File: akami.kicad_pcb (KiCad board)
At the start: 4 copper layers, 30 x 33.3 mm, 64 parts, among them J1 USB_C_Receptacle_USB2.0, J2 Conn_01x01, J3 Conn_01x01, Q2 AO3401A, U1 nRF52840, U2 TP4054, U3 LP5912-3.3DRV, U4 ProMicro_2, Y1 32MHz, Y2 32.768 kHz

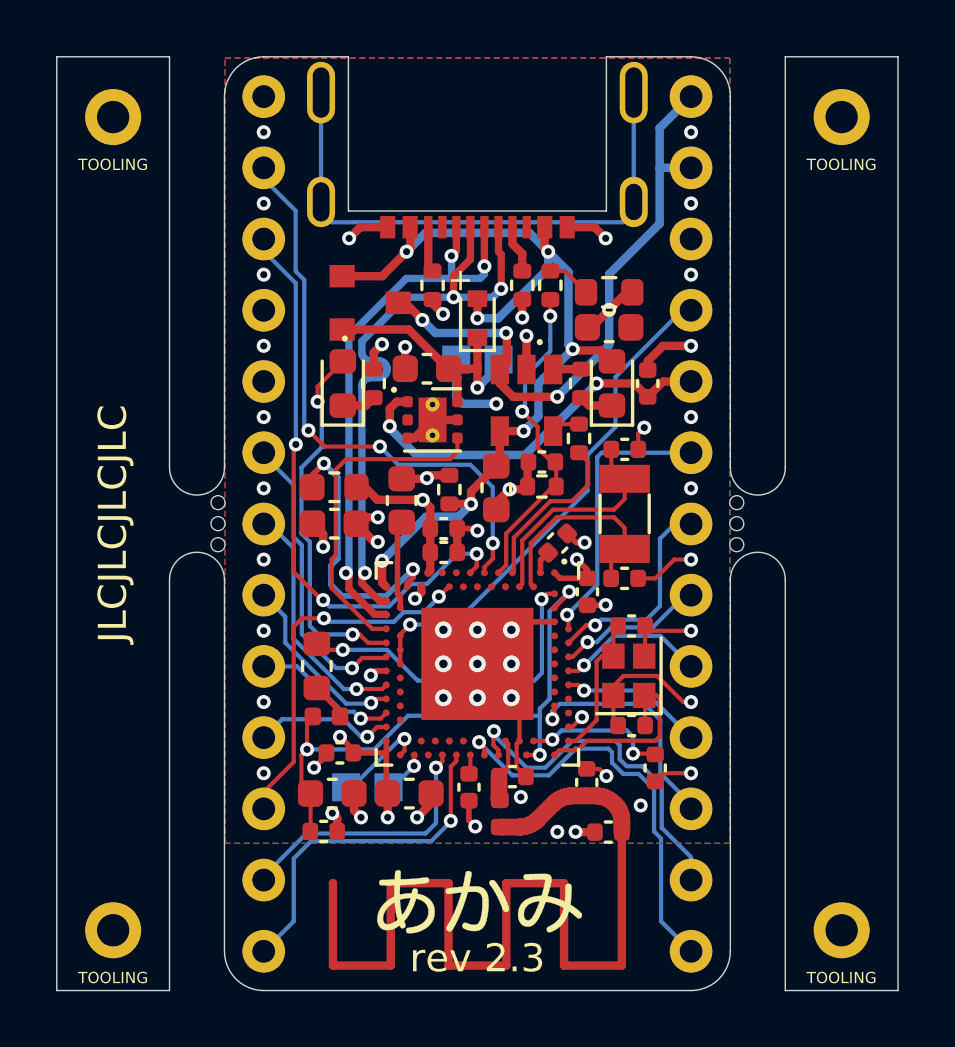
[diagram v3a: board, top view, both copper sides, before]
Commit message: continue placement and routing on 3A
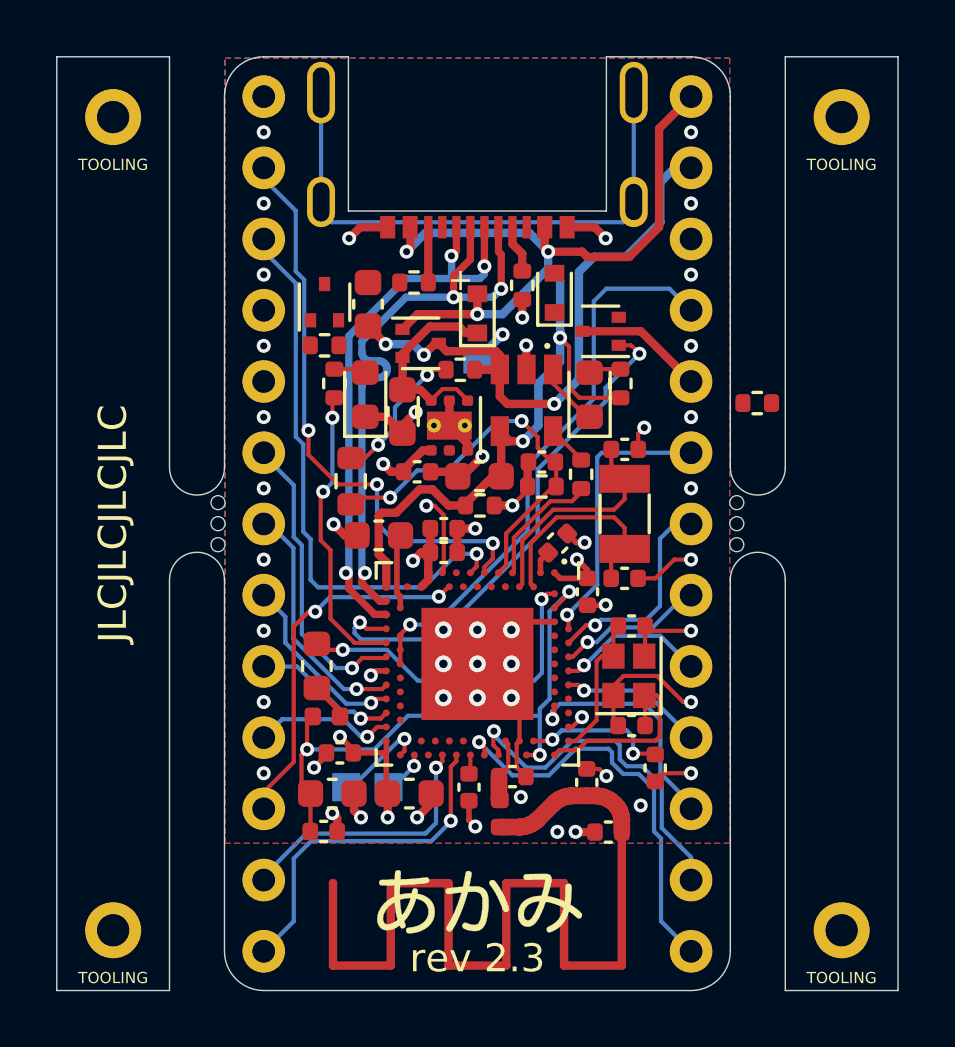
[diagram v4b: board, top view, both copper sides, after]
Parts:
- removed C23: 4.7uF, Capacitor_SMD:C_0603_1608Metric
- removed L4: 10uH, Inductor_SMD:L_0603_1608Metric
- removed TP5: TestPoint, TestPoint:TestPoint_Pad_1.0x1.0mm
- added D4: MSK4010, Diode_SMD:D_SOD-523, F.Cu at (2.75, -8.23)
- added Q1: DMP21D0UT, Package_TO_SOT_SMD:SOT-523, F.Cu at (4.39, -6.86)
- added Q3: DMP21D0UT, Package_TO_SOT_SMD:SOT-523, F.Cu at (-5.45, -7.90)
- added R1: 100k, Resistor_SMD:R_0402_1005Metric, F.Cu at (9.98, -4.30)
- added R2: 100k, Resistor_SMD:R_0402_1005Metric, F.Cu at (-5.45, -6.36)
- D2: value 1N5817 -> MSK4010
- Q2: value AO3401A -> DMP21D0UT; footprint Package_TO_SOT_SMD:SOT-23 -> Package_TO_SOT_SMD:SOT-523
- moved R11 11.4 mm to (-4.52, -1.51), turned to 270 degrees
- moved C24 8.81 mm to (-2.15, -1.85), turned to 0 degrees
- moved C21 8.64 mm to (-3.90, -7.83), turned to 270 degrees
- moved R3 4.40 mm to (-0.61, -5.49), turned to 180 degrees
- moved Q2 2.31 mm to (-2.02, -6.43)
- moved C20 1.76 mm to (-2.67, -4.00), turned to 90 degrees
- moved C13 1.49 mm to (-3.52, 0.42), turned to 180 degrees
- moved R5 1.40 mm to (-5.10, -5.00)
- moved R8 1.40 mm to (5.10, -5.00)
- moved R7 1.28 mm to (3.70, -1.76)
- moved R6 1.23 mm to (0.09, -0.65), turned to 0 degrees
- moved D1 0.89 mm to (-4.00, -4.60)
- moved D3 0.89 mm to (4.00, -4.60)
- moved TP3 0.76 mm to (0.00, -5.85)
- moved C14 0.73 mm to (0.07, -1.69), turned to 0 degrees
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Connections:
- C20 pad 2: VDD_HV -> Net-(C20-Pad2)
- C24 pad 1: EXT_VCC -> VDD_NRF
- D1 pad 1: Net-(D1-Pad1) -> GND
- D1 pad 2: BLUE_LED -> Net-(D1-Pad2)
- D2 pad 1: VDD_HV -> Net-(C20-Pad2)
- D3 pad 2: VBUS -> Net-(D3-Pad2)
- J2 pad 1: VBAT -> VBUS
- J3 pad 1: GND -> EXT_VCC
- Q2 pad 2: VDD_HV -> Net-(C20-Pad2)
- R11 pad 1: VBAT -> Net-(R11-Pad1)
- R11 pad 2: Net-(R11-Pad2) -> BAT_VOLT
- R3 pad 1: Net-(R11-Pad2) -> VBAT
- R3 pad 2: BAT_VOLT -> Net-(R11-Pad1)
- R5 pad 1: GND -> Net-(D1-Pad2)
- R5 pad 2: Net-(D1-Pad1) -> BLUE_LED
- R8 pad 1: Net-(R8-Pad1) -> Net-(D3-Pad2)
- R8 pad 2: Net-(D3-Pad1) -> VBUS
- U1 pad AD8: POWER_CTRL -> PPH_VCC_CTRL
- U1 pad Y2: VDD_HV -> VDD_NRF
- U2 pad 1: Net-(R8-Pad1) -> Net-(D3-Pad1)
- U3 pad 1: EXT_VCC -> VDD_NRF
- U3 pad 4: POWER_CTRL -> Net-(C20-Pad2)
- U3 pad 6: VDD_HV -> Net-(C20-Pad2)
- U4 pad 21: EXT_VCC -> PPH_VCC
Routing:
- net VDD_HV: track 23.4 -> 0.00 mm, vias 4 -> 0
- net PPH_VCC_CTRL: track 0.00 -> 19.2 mm, vias 0 -> 2
- net EXT_VCC: track 14.1 -> 0.00 mm, vias 2 -> 0
- net VBUS: track 33.4 -> 45.8 mm, vias 7 -> 5
- net POWER_CTRL: track 11.9 -> 0.00 mm
- net Net-(U1-PadAB2): track 9.85 -> 0.00 mm, vias 2 -> 0
- net Net-(C20-Pad2): track 0.00 -> 7.30 mm
- net Net-(R11-Pad1): track 0.00 -> 5.14 mm, vias 0 -> 2
- net PPH_VCC: track 0.00 -> 4.61 mm
- net VBAT: track 24.4 -> 21.4 mm, vias 4 -> 3
- net Net-(U1-PadU1): track 0.00 -> 2.84 mm, vias 0 -> 1
- net BLUE_LED: track 13.3 -> 10.6 mm
- net BAT_VOLT: track 11.6 -> 14.2 mm
- net RESET: track 18.0 -> 20.3 mm
- net GND: track 40.5 -> 38.5 mm, vias 53 -> 51
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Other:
- board text added: "VCC"
- board text removed: "H"
- board text removed: "L"

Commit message: rev 3 (lv): 1. layout and route all components
2. replace mosfet pullups with 1M resistors

3. silkscreen pin labelling now shows nRF52 pin numbers instead
   of promicro pins (those are "standard" and hence useless to
   print)

4. VBUS and EXT_VCC is now broken out; VBUS is coincidentally in
   the same place as an Elite-C (above RAW -- now BAT)

gerbers, BOM, and PnP files *are* updated.
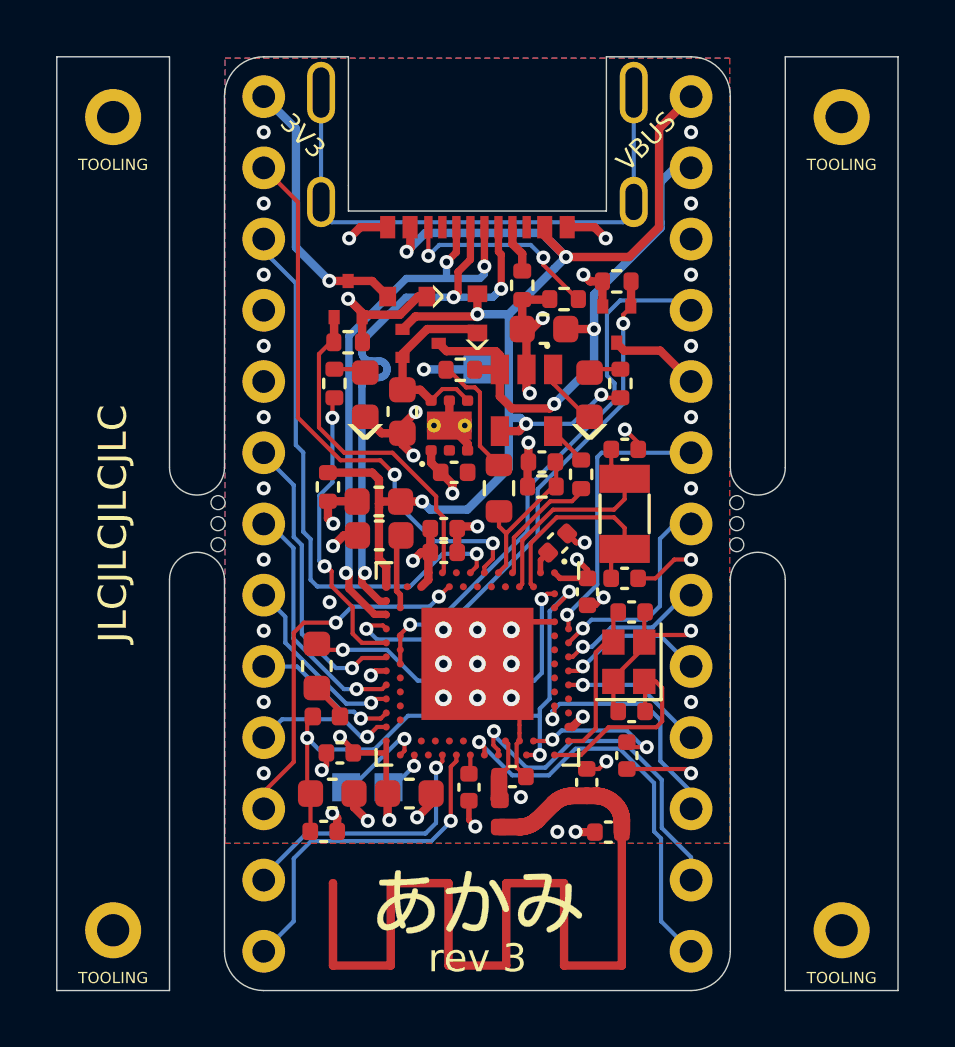
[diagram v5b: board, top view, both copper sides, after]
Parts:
- R1, R2: value 100k -> 1M
- U4: footprint footprints:promicro_no_silk -> footprints:akami-pins
- moved R1 6.63 mm to (4.97, -8.64)
- moved C21 6.34 mm to (2.38, -6.94), turned to 0 degrees
- moved R6 5.46 mm to (-5.33, -1.31), turned to 270 degrees
- moved R10 5.38 mm to (3.09, -8.01)
- moved R11 5.30 mm to (0.77, -1.26)
- moved D4 5.25 mm to (-2.50, -8.10), turned to 180 degrees
- moved C14 3.70 mm to (-3.52, -0.79)
- moved C24 1.32 mm to (-0.83, -1.83)
- moved C11 1.10 mm to (5.33, 8.27)
- moved Q3 0.85 mm to (-4.61, -8.01)
- moved R2 0.85 mm to (-4.61, -6.47)
- moved Q1 0.62 mm to (4.97, -7.10), turned to 270 degrees
- moved C6 0.50 mm to (5.50, 6.70)
- moved C7 0.50 mm to (5.50, 3.15)
- moved Y1 0.50 mm to (5.40, 4.92)
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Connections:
- net P1.10 renamed Net-(U1-PadA20)
- U1 pad U1: Net-(U1-PadU1) -> EXT_VCC_CTRL
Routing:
- net EXT_VCC_CTRL: track 0.00 -> 12.3 mm
- net EXT_VCC: track 0.00 -> 9.85 mm, vias 0 -> 1
- net BAT_VOLT: track 14.2 -> 5.78 mm, vias 2 -> 0
- net VDD_NRF: track 14.4 -> 21.0 mm, vias 8 -> 10
- net Net-(J1-PadB5): track 1.97 -> 7.50 mm, vias 0 -> 2
- net GND: track 38.5 -> 41.8 mm, vias 51 -> 52
- net Net-(U1-PadU1): track 2.84 -> 0.00 mm, vias 1 -> 0
- net VBAT: track 21.4 -> 18.7 mm, vias 3 -> 2
- net VBUS: track 45.8 -> 47.3 mm, vias 5 -> 6
- net PPH_VCC: track 4.61 -> 3.24 mm
- net P0.06: track 20.8 -> 20.0 mm, vias 3 -> 2
- net Net-(R11-Pad1): track 5.14 -> 4.42 mm, vias 2 -> 0
- net RESET: track 20.3 -> 19.6 mm
- net Net-(C7-Pad1): track 5.23 -> 5.79 mm
- net PPH_VCC_CTRL: track 19.2 -> 19.8 mm
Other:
- board text added: "3V3"
- board text added: "VBUS"
- board text added: "^"
- board text added: "rev 3"
- board text removed: "+"
- board text removed: "rev 2.3"

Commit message: rev 3.1 (lv):
1. move the antenna down slightly.
2. adjust thermal spoke fill parameters on the front copper
   around the transmission line.
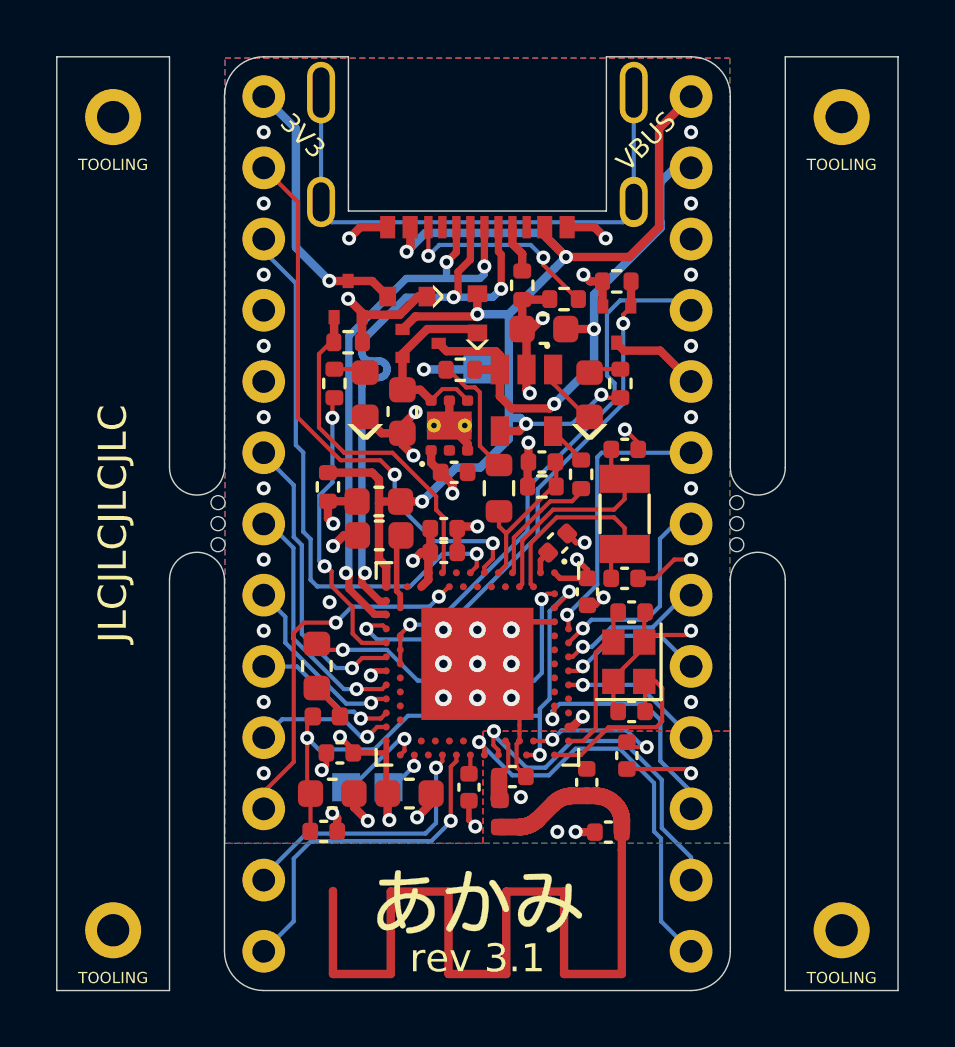
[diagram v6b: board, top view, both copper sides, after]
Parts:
- moved TP4 0.28 mm to (-5.15, 13.1)
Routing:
- net VBUS: track 47.3 -> 46.4 mm
- net GND: track 41.8 -> 41.0 mm, vias 52 -> 51
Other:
- board text added: "rev 3.1"
- board text removed: "rev 3"

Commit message: rev 3.2
1. re-layout and re-route the entire thing
2. as part of (1), move the nrf chip up by 0.75mm
3. add a 1uF capacitor on the VBUS input to the charger IC
4. move components further away from the USB connector since that
   has to be hand-soldered
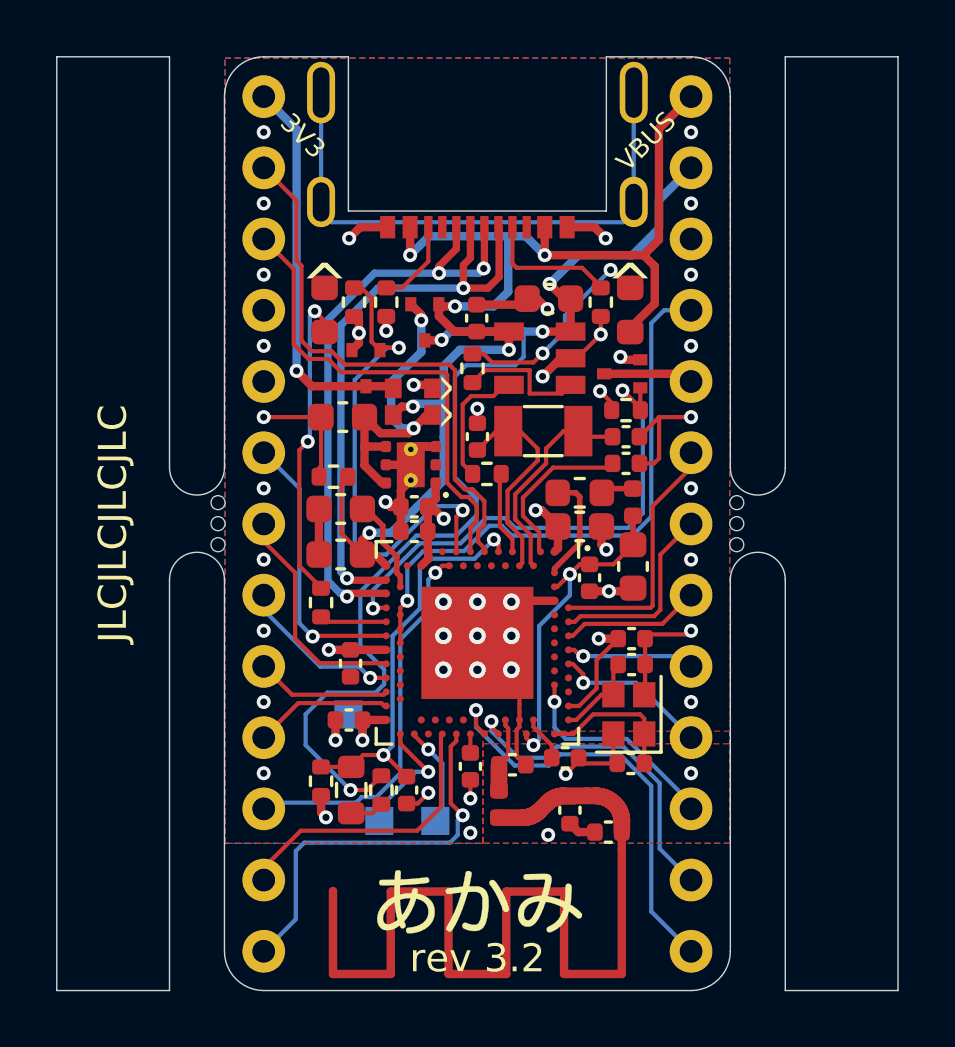
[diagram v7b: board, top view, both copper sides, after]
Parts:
- removed DUMMY5, DUMMY6, DUMMY7, DUMMY8: tooling_hole, footprints:jlcpcb_tooling_hole
- added C23: 1uF, Capacitor_SMD:C_0402_1005Metric, F.Cu at (-0.03, -7.33)
- moved R3 15.3 mm to (-3.42, 9.50), turned to 270 degrees
- moved C16 13.4 mm to (5.55, 1.52), turned to 90 degrees
- moved L2 13.3 mm to (5.55, -0.77), turned to 90 degrees
- moved R4 13.1 mm to (-5.58, 9.19), turned to 270 degrees
- moved TP3 13.1 mm to (-4.60, 6.80)
- moved C15 13.1 mm to (4.00, 1.93), turned to 90 degrees
- moved C19 12.7 mm to (-2.52, 9.50), turned to 90 degrees
- moved R11 12.0 mm to (-4.50, 9.50), turned to 90 degrees
- moved C1 11.3 mm to (3.65, 0.10)
- moved L3 11.2 mm to (3.65, -1.10), turned to 180 degrees
- moved C3 11.2 mm to (5.50, 4.10), turned to 180 degrees
- moved C4 8.83 mm to (-4.53, 4.98)
- moved R5 7.83 mm to (-5.58, 2.81)
- moved C2 6.86 mm to (-4.58, 7.00), turned to 0 degrees
- moved R10 6.34 mm to (-3.25, -7.90), turned to 270 degrees
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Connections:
- D3 pad 2: Net-(D3-Pad2) -> VBUS
- R8 pad 1: Net-(D3-Pad2) -> Net-(R8-Pad1)
- R8 pad 2: VBUS -> Net-(D3-Pad1)
- U1 pad R1: Net-(U1-PadR1) -> EXT_VCC_CTRL
- U1 pad U1: EXT_VCC_CTRL -> Net-(U1-PadU1)
- U2 pad 1: Net-(D3-Pad1) -> Net-(R8-Pad1)
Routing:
- net VBAT: track 18.7 -> 40.6 mm, vias 2 -> 4
- net Net-(D1-Pad2): track 1.15 -> 11.3 mm, vias 0 -> 2
- net Net-(C15-Pad2): track 20.7 -> 11.6 mm, vias 3 -> 2
- net BAT_VOLT: track 5.78 -> 14.4 mm, vias 0 -> 2
- net BLUE_LED: track 10.5 -> 2.40 mm, vias 2 -> 0
- net Net-(L3-Pad2): track 11.9 -> 3.93 mm, vias 2 -> 0
- net EXT_VCC_CTRL: track 12.3 -> 17.7 mm, vias 0 -> 2
- net Net-(D3-Pad1): track 2.38 -> 7.70 mm, vias 0 -> 2
- net Net-(C10-Pad1): track 0.83 -> 5.89 mm
- net Net-(C20-Pad2): track 7.22 -> 12.1 mm, vias 0 -> 2
- net Net-(R8-Pad1): track 0.00 -> 4.68 mm
- net Net-(J1-PadB5): track 7.50 -> 3.11 mm, vias 2 -> 0
- net EXT_VCC: track 9.85 -> 14.0 mm
- net Net-(C11-Pad1): track 5.23 -> 1.62 mm, vias 2 -> 0
- net Net-(R11-Pad1): track 4.42 -> 1.21 mm
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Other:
- board text added: "C"
- board text added: "D"
- board text added: "rev 3.2"
- board text removed: "SWC"
- board text removed: "SWD"
- board text removed: "rev 3.1"
